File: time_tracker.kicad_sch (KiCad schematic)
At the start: 15 parts, among them U1 max7219cng, U2 max7219cng, U3 XIAO ESP32C3

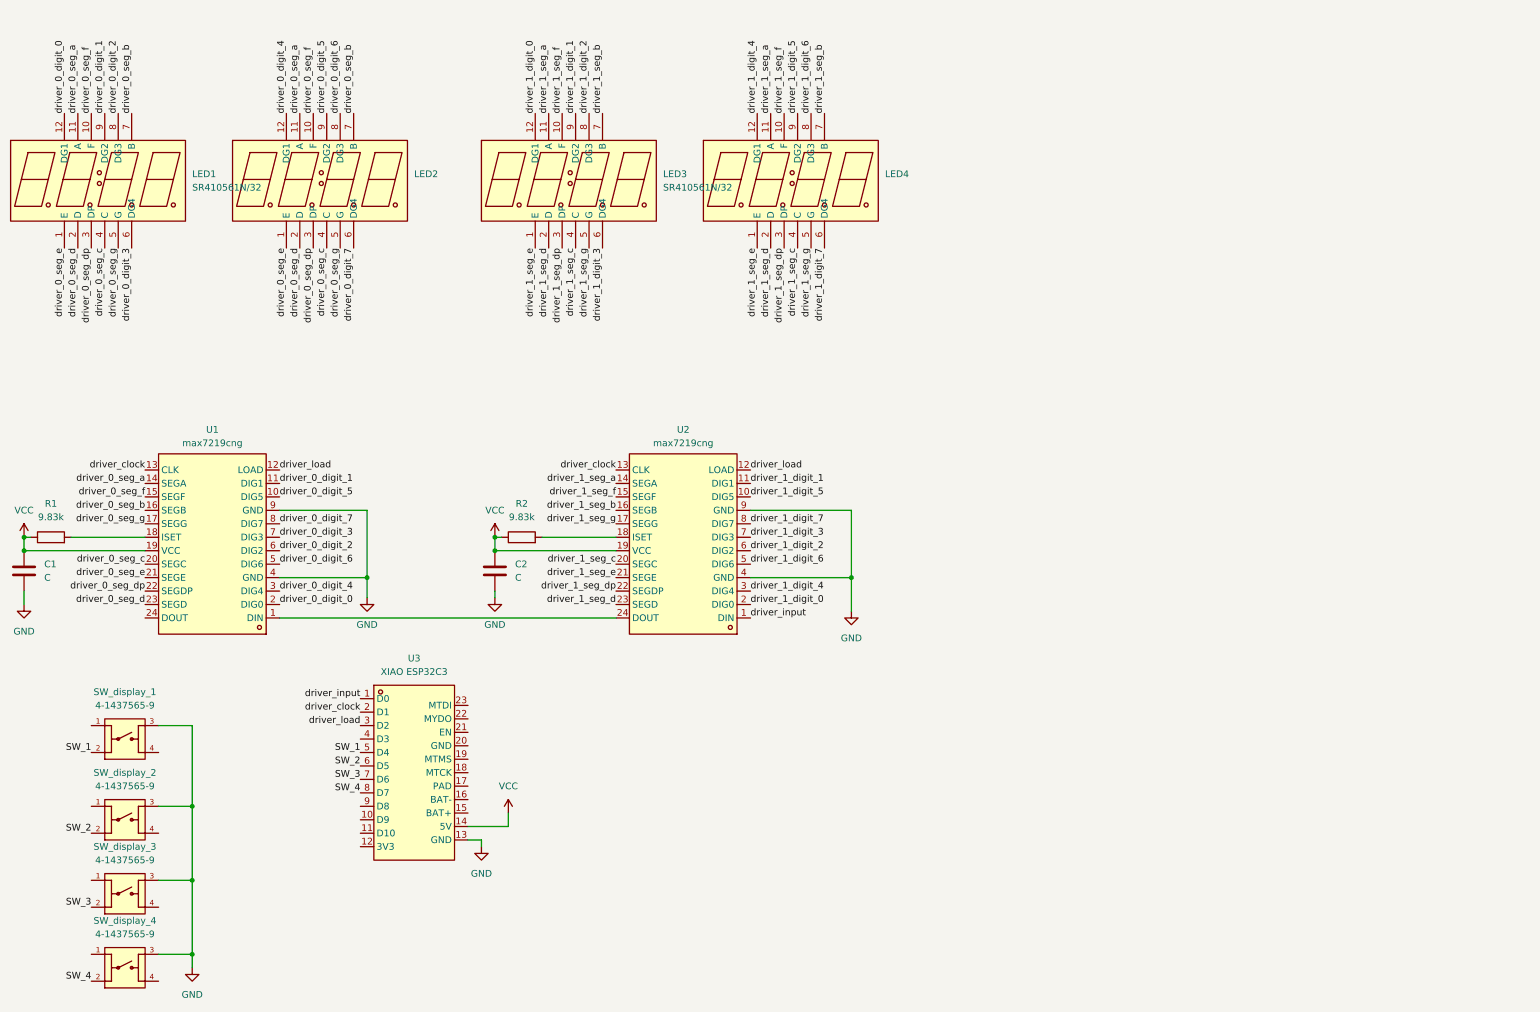
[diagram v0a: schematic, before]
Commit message: added rtc, battery circuit
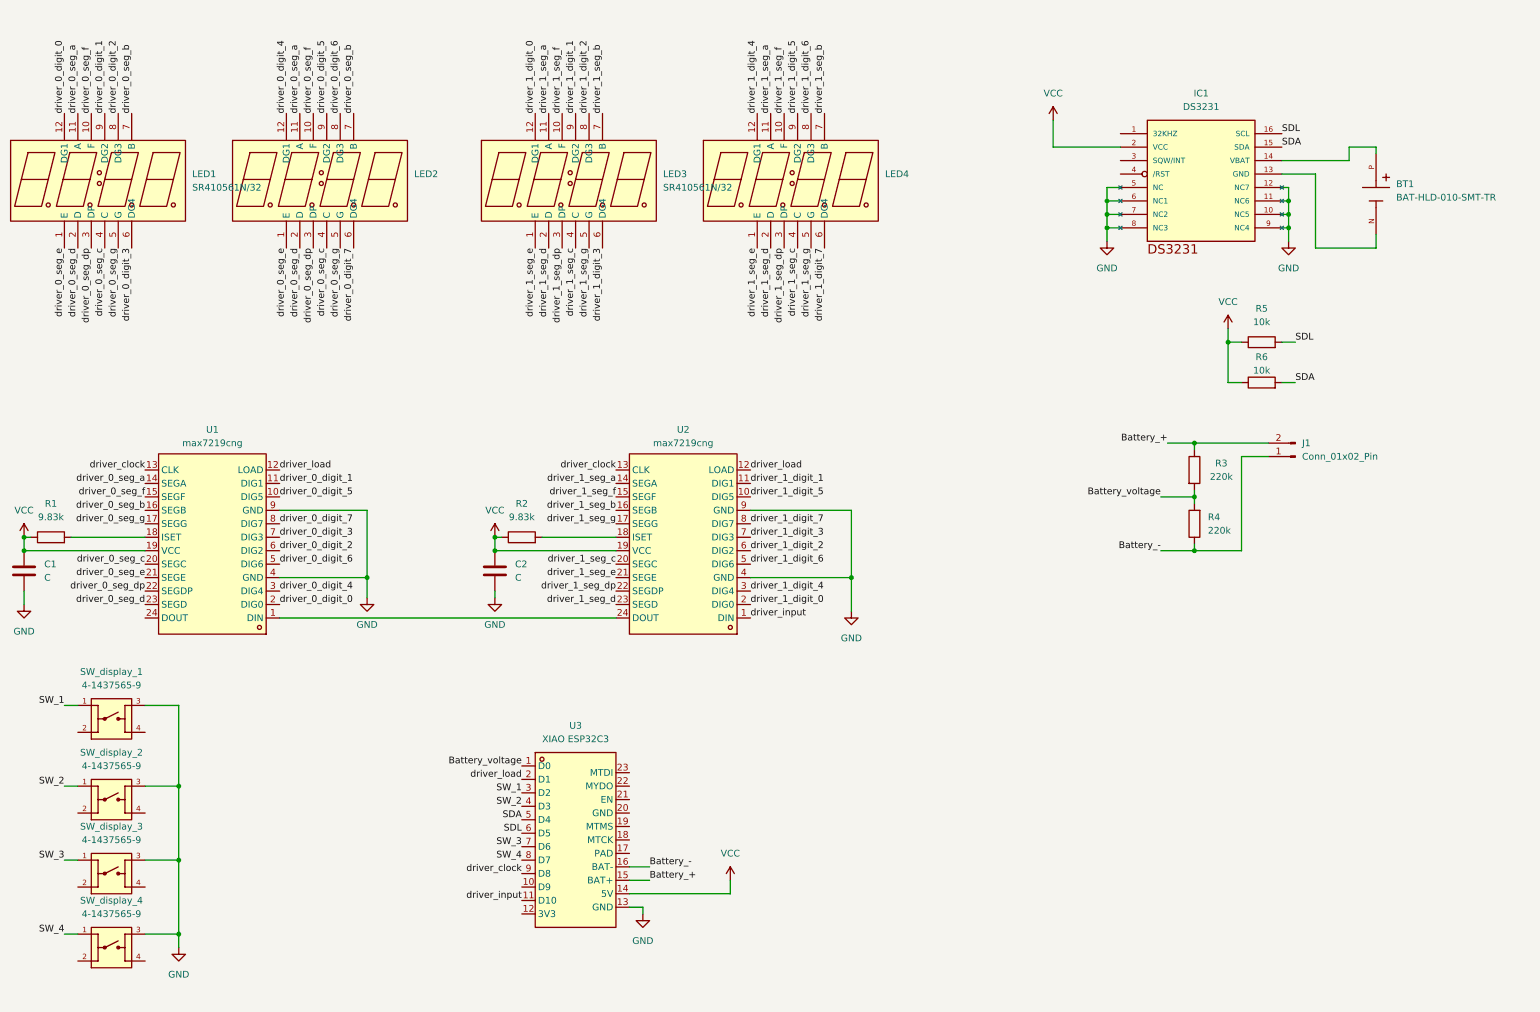
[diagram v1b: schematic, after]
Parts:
- added BT1: BAT-HLD-010-SMT-TR, cr2032 holder:BAT_BAT-HLD-010-SMT-TR, symbol cr2032:BAT-HLD-010-SMT-TR
- added IC1: DS3231, DS3231:SO16W, symbol DS3231:DS3231
- added J1: Conn_01x02_Pin, Connector_PinHeader_2.54mm:PinHeader_1x02_P2.54mm_Vertical, symbol Connector:Conn_01x02_Pin
- added R3, R4: 220k, Resistor_SMD:R_1206_3216Metric, symbol Device:R
- added R5, R6: 10k, Resistor_SMD:R_1206_3216Metric, symbol Device:R
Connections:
- net GND: now also IC1.10 (NC5), IC1.11 (NC6), IC1.12 (NC7), IC1.5 (NC), IC1.6 (NC1), IC1.7 (NC2), IC1.8 (NC3), IC1.9 (NC4)
- net SW_1: now also SW_display_1.1, U3.3 (D2); no longer SW_display_1.2, U3.5 (D4)
- net SW_2: now also SW_display_2.1, U3.4 (D3); no longer SW_display_2.2, U3.6 (D5)
- net SW_3: now also SW_display_3.1; no longer SW_display_3.2
- net SW_4: now also SW_display_4.1; no longer SW_display_4.2
- net VCC: now also IC1.2 (VCC), R5.1, R6.1
- net driver_clock: now also U3.9 (D8); no longer U3.2 (D1)
- net driver_input: now also U3.11 (D10); no longer U3.1 (D0)
- net driver_load: now also U3.2 (D1); no longer U3.3 (D2)
- net Battery_+: now reaches U3.15 (BAT+)
- net Battery_+: now also J1.2 (Pin_2), R3.1
- net Battery_-: now reaches U3.16 (BAT-)
- net Battery_-: now also J1.1 (Pin_1), R4.1
- new net: BT1.N, IC1.13 (GND)
- new net: BT1.P, IC1.14 (VBAT)
- new net Battery_voltage: R3.2, R4.2, U3.1 (D0)
- new net SDA: IC1.15 (SDA), R6.2, U3.5 (D4)
- new net SDL: IC1.16 (SCL), R5.2, U3.6 (D5)
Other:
- moved on the sheet: SW_display_1, SW_display_2, SW_display_3, SW_display_4, U3
